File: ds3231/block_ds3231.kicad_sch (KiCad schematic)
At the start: 6 parts, among them U1 DS3231M

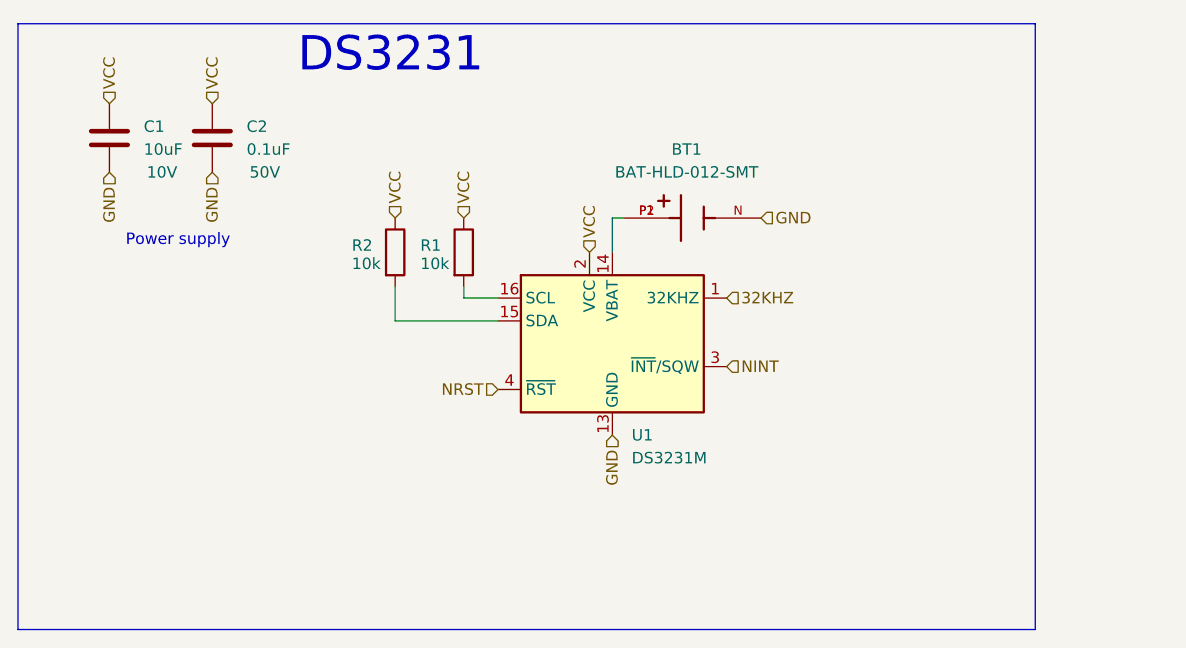
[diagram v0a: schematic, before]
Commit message: [Rushil] corrected pcb added information on both schematic and pcb user drawing correct circuit of bno055
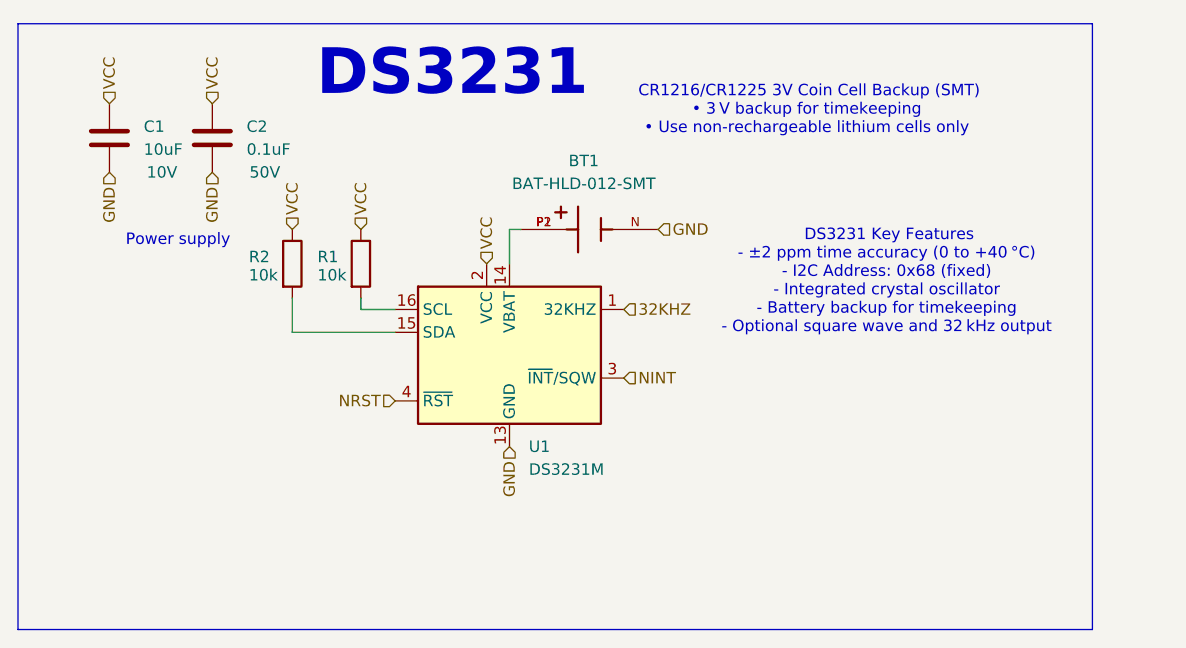
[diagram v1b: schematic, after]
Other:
- note added: "CR1216/CR1225 3V Coin Cell Backup (SMT) • 3 V backup for timekeeping • Use non-rechargeable lithium cells only"
- note added: "DS3231 Key Features - ±2 ppm time accuracy (0 to +40 °C) - I2C Address: 0x68 (fixed) - Integrated crystal oscillator - Battery backup for timekeeping - Optional square wave and 32 kHz output"
- moved on the sheet: BT1, R1, R2, U1
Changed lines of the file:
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@@
 	(rectangle
 		(start 81.28 57.15)
-		(end 194.31 124.46)
+		(end 200.66 124.46)
 		(stroke
 			(width 0)
@@
 		)
 	)
+	(text " DS3231 Key Features  \n- ±2 ppm time accuracy (0 to +40 °C)  \n- I2C Address: 0x68 (fixed)  \n- Integrated crystal oscillator  \n- Battery backup for timekeeping  \n- Optional square wave and 32 kHz output"
+		(exclude_from_sim no)
+		(at 177.8 85.852 0)
+		(effects
+			(font
+				(size 1.27 1.27)
+			)
+		)
+	)
 	(text "Power supply\n"
 		(exclude_from_sim no)
@@
 		)
 	)
-	(text "DS3231\n"
-		(exclude_from_sim no)
-		(at 122.682 60.706 0)
-		(effects
-			(font
-				(size 3.81 3.81)
+	(text " CR1216/CR1225 3V Coin Cell Backup (SMT)\n• 3 V backup for timekeeping  \n• Use non-rechargeable lithium cells only\n"
+		(exclude_from_sim no)
+		(at 168.91 66.802 0)
+		(effects
+			(font
+				(size 1.27 1.27)
+			)
+		)
+	)
+	(text "DS3231"
+		(exclude_from_sim no)
+		(at 129.54 62.738 0)
+		(effects
+			(font
+				(size 5.08 5.08)
+				(thickness 1.016)
+				(bold yes)
 			)
 		)
@@
 	(wire
 		(pts
-			(xy 123.19 90.17) (xy 134.62 90.17)
+			(xy 111.76 91.44) (xy 123.19 91.44)
 		)
 		(stroke
@@
 	(wire
 		(pts
-			(xy 147.32 78.74) (xy 147.32 82.55)
+			(xy 135.89 80.01) (xy 135.89 83.82)
 		)
 		(stroke
@@
 	(wire
 		(pts
-			(xy 148.59 78.74) (xy 147.32 78.74)
+			(xy 137.16 80.01) (xy 135.89 80.01)
 		)
 		(stroke
@@
 	(wire
 		(pts
-			(xy 130.81 87.63) (xy 130.81 86.36)
+			(xy 119.38 88.9) (xy 119.38 87.63)
 		)
 		(stroke
@@
 	(wire
 		(pts
-			(xy 123.19 86.36) (xy 123.19 90.17)
+			(xy 111.76 87.63) (xy 111.76 91.44)
 		)
 		(stroke
@@
 	(wire
 		(pts
-			(xy 130.81 87.63) (xy 134.62 87.63)
+			(xy 119.38 88.9) (xy 123.19 88.9)
 		)
 		(stroke
@@
 	(hierarchical_label "GND"
 		(shape input)
-		(at 147.32 102.87 270)
+		(at 135.89 104.14 270)
 		(effects
 			(font
@@
 	(hierarchical_label "NINT"
 		(shape input)
-		(at 160.02 95.25 0)
+		(at 148.59 96.52 0)
 		(effects
 			(font
@@
 	(hierarchical_label "GND"
 		(shape input)
-		(at 163.83 78.74 0)
+		(at 152.4 80.01 0)
 		(effects
 			(font
@@
 	(hierarchical_label "NRST"
 		(shape input)
-		(at 134.62 97.79 180)
+		(at 123.19 99.06 180)
 		(effects
 			(font
@@
 	(hierarchical_label "VCC"
 		(shape input)
-		(at 144.78 82.55 90)
+		(at 133.35 83.82 90)
 		(effects
 			(font
@@
 	(hierarchical_label "32KHZ"
 		(shape input)
-		(at 160.02 87.63 0)
+		(at 148.59 88.9 0)
 		(effects
 			(font
@@
 	(hierarchical_label "VCC"
 		(shape input)
-		(at 130.81 78.74 90)
+		(at 119.38 80.01 90)
 		(effects
 			(font
@@
 	(hierarchical_label "VCC"
 		(shape input)
-		(at 123.19 78.74 90)
+		(at 111.76 80.01 90)
 		(effects
 			(font
@@
 	(symbol
 		(lib_id "Library:R")
-		(at 123.19 82.55 0)
+		(at 111.76 83.82 0)
 		(unit 1)
 		(exclude_from_sim no)
@@
 		(dnp no)
 		(property "Reference" "R2"
-			(at 118.364 81.788 0)
+			(at 106.934 83.058 0)
 			(effects
 				(font
@@
 		)
 		(property "Value" "10k"
-			(at 118.364 83.82 0)
+			(at 106.934 85.09 0)
 			(effects
 				(font
@@
 		)
 		(property "Footprint" "Resistor_SMD:R_0603_1608Metric"
-			(at 121.412 82.55 90)
+			(at 109.982 83.82 90)
 			(effects
 				(font
@@
 		)
 		(property "Datasheet" "~"
-			(at 123.19 82.55 0)
+			(at 111.76 83.82 0)
 			(effects
 				(font
@@
 		)
 		(property "Description" "Resistor"
-			(at 123.19 82.55 0)
+			(at 111.76 83.82 0)
 			(effects
 				(font
@@
 		)
 		(property "package" "0603"
-			(at 123.19 82.55 0)
+			(at 111.76 83.82 0)
 			(effects
 				(font
@@
 		)
 		(property "LCSC_part#" "C25804"
-			(at 123.19 82.55 0)
+			(at 111.76 83.82 0)
 			(effects
 				(font
@@
 		)
 		(property "MPN" "0603WAF1002T5E"
-			(at 123.19 82.55 0)
+			(at 111.76 83.82 0)
 			(effects
 				(font
@@
 		)
 		(instances
-			(project "ds3231_rtc"
+			(project "ds3231"
 				(path "/2bca7139-9750-4f0a-8cae-c77d5e9ee787/2158ea61-c96a-4c98-b294-c4fdff84ada6"
 					(reference "R2")
@@
 		)
 		(instances
-			(project "ds3231_rtc"
+			(project "ds3231"
 				(path "/2bca7139-9750-4f0a-8cae-c77d5e9ee787/2158ea61-c96a-4c98-b294-c4fdff84ada6"
 					(reference "C1")
@@
 	(symbol
 		(lib_id "Library:R")
-		(at 130.81 82.55 0)
+		(at 119.38 83.82 0)
 		(unit 1)
 		(exclude_from_sim no)
@@
 		(dnp no)
 		(property "Reference" "R1"
-			(at 125.984 81.788 0)
+			(at 114.554 83.058 0)
 			(effects
 				(font
@@
 		)
 		(property "Value" "10k"
-			(at 125.984 83.82 0)
+			(at 114.554 85.09 0)
 			(effects
 				(font
@@
 		)
 		(property "Footprint" "Resistor_SMD:R_0603_1608Metric"
-			(at 129.032 82.55 90)
+			(at 117.602 83.82 90)
 			(effects
 				(font
@@
 		)
 		(property "Datasheet" "~"
-			(at 130.81 82.55 0)
+			(at 119.38 83.82 0)
 			(effects
 				(font
@@
 		)
 		(property "Description" "Resistor"
-			(at 130.81 82.55 0)
+			(at 119.38 83.82 0)
 			(effects
 				(font
@@
 		)
 		(property "package" "0603"
-			(at 130.81 82.55 0)
+			(at 119.38 83.82 0)
 			(effects
 				(font
@@
 		)
 		(property "LCSC_part#" "C25804"
-			(at 130.81 82.55 0)
+			(at 119.38 83.82 0)
 			(effects
 				(font
@@
 		)
 		(property "MPN" "0603WAF1002T5E"
-			(at 130.81 82.55 0)
+			(at 119.38 83.82 0)
 			(effects
 				(font
@@
 		)
 		(instances
-			(project "ds3231_rtc"
+			(project "ds3231"
 				(path "/2bca7139-9750-4f0a-8cae-c77d5e9ee787/2158ea61-c96a-4c98-b294-c4fdff84ada6"
 					(reference "R1")
@@
 		)
 		(instances
-			(project "ds3231_rtc"
+			(project "ds3231"
 				(path "/2bca7139-9750-4f0a-8cae-c77d5e9ee787/2158ea61-c96a-4c98-b294-c4fdff84ada6"
 					(reference "C2")
@@
 	(symbol
 		(lib_id "Library:DS3231M")
-		(at 147.32 92.71 0)
+		(at 135.89 93.98 0)
 		(unit 1)
 		(exclude_from_sim no)
@@
 		(fields_autoplaced yes)
 		(property "Reference" "U1"
-			(at 149.4633 102.87 0)
+			(at 138.0333 104.14 0)
 			(effects
 				(font
@@
 		)
 		(property "Value" "DS3231M"
-			(at 149.4633 105.41 0)
+			(at 138.0333 106.68 0)
 			(effects
 				(font
@@
 		)
 		(property "Footprint" "Package_SO:SOIC-16W_7.5x10.3mm_P1.27mm"
-			(at 147.32 107.95 0)
+			(at 135.89 109.22 0)
 			(effects
 				(font
@@
 		)
 		(property "Datasheet" "http://datasheets.maximintegrated.com/en/ds/DS3231.pdf"
-			(at 154.178 91.44 0)
+			(at 142.748 92.71 0)
 			(effects
 				(font
@@
 		)
 		(property "Description" "Extremely Accurate I2C-Integrated RTC/TCXO/Crystal SOIC-16"
-			(at 147.32 92.71 0)
+			(at 135.89 93.98 0)
 			(effects
 				(font
@@
 		)
 		(property "LCSC_part#" "C37663"
-			(at 147.32 92.71 0)
+			(at 135.89 93.98 0)
 			(effects
 				(font
@@
 		)
 		(property "MPN" "DS3231M+TRL"
-			(at 147.32 92.71 0)
+			(at 135.89 93.98 0)
 			(effects
 				(font
@@
 		)
 		(instances
-			(project ""
+			(project "ds3231"
 				(path "/2bca7139-9750-4f0a-8cae-c77d5e9ee787/2158ea61-c96a-4c98-b294-c4fdff84ada6"
 					(reference "U1")
@@
 	(symbol
 		(lib_id "Library:BAT-HLD-012-SMT")
-		(at 156.21 78.74 0)
+		(at 144.78 80.01 0)
 		(unit 1)
 		(exclude_from_sim no)
@@
 		(fields_autoplaced yes)
 		(property "Reference" "BT1"
-			(at 155.575 71.12 0)
+			(at 144.145 72.39 0)
 			(effects
 				(font
@@
 		)
 		(property "Value" "BAT-HLD-012-SMT"
-			(at 155.575 73.66 0)
+			(at 144.145 74.93 0)
 			(effects
 				(font
@@
 		)
 		(property "Footprint" "BAT-HLD-012-SMT:BAT_BAT-HLD-012-SMT"
-			(at 156.21 78.74 0)
+			(at 144.78 80.01 0)
 			(effects
 				(font
@@
 		)
 		(property "Datasheet" ""
-			(at 156.21 78.74 0)
+			(at 144.78 80.01 0)
 			(effects
 				(font
@@
 		)
 		(property "Description" ""
-			(at 156.21 78.74 0)
+			(at 144.78 80.01 0)
 			(effects
 				(font
@@
 		)
 		(property "LCSC_part#" "C5189234"
-			(at 156.21 78.74 0)
+			(at 144.78 80.01 0)
 			(effects
 				(font
@@
 		)
 		(property "MPN" "BAT-HLD-012-SMT"
-			(at 156.21 78.74 0)
+			(at 144.78 80.01 0)
 			(effects
 				(font
@@
 		)
 		(instances
-			(project ""
+			(project "ds3231"
 				(path "/2bca7139-9750-4f0a-8cae-c77d5e9ee787/2158ea61-c96a-4c98-b294-c4fdff84ada6"
 					(reference "BT1")

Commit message: [Rushil] added ams1117-3.3 block and did some clean up in schematic info part
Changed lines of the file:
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@@
 	(text " DS3231 Key Features  \n- ±2 ppm time accuracy (0 to +40 °C)  \n- I2C Address: 0x68 (fixed)  \n- Integrated crystal oscillator  \n- Battery backup for timekeeping  \n- Optional square wave and 32 kHz output"
 		(exclude_from_sim no)
-		(at 177.8 85.852 0)
+		(at 158.242 89.662 0)
 		(effects
 			(font
 				(size 1.27 1.27)
 			)
+			(justify left)
 		)
 	)
@@
 	(text " CR1216/CR1225 3V Coin Cell Backup (SMT)\n• 3 V backup for timekeeping  \n• Use non-rechargeable lithium cells only\n"
 		(exclude_from_sim no)
-		(at 168.91 66.802 0)
+		(at 155.448 102.108 0)
 		(effects
 			(font
 				(size 1.27 1.27)
 			)
+			(justify left)
 		)
 	)

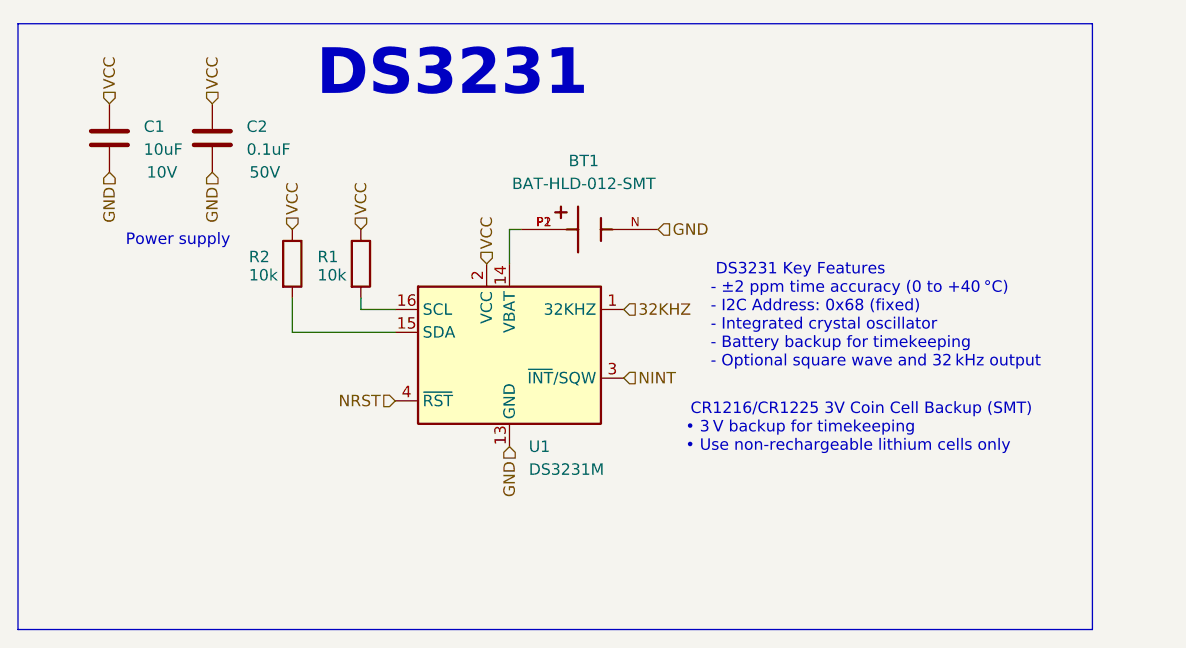
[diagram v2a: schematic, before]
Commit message: Edited and finalized blocks MCP9809 and DS3231
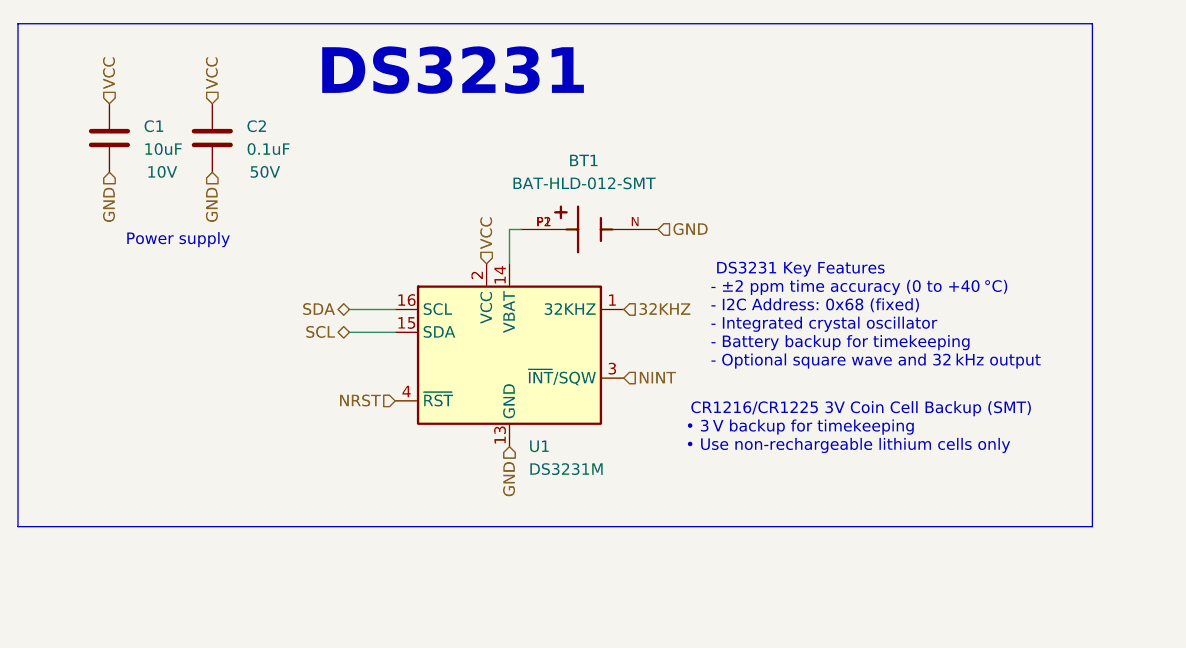
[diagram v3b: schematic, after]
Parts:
- removed R1, R2: 10k, Resistor_SMD:R_0603_1608Metric, symbol Library:R
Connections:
- net SCL: now reaches U1.15 (SDA)
- net SDA: now reaches U1.16 (SCL)
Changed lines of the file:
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@@
 	(rectangle
 		(start 81.28 57.15)
-		(end 200.66 124.46)
+		(end 200.66 113.03)
 		(stroke
 			(width 0)
@@
 	(wire
 		(pts
-			(xy 111.76 91.44) (xy 123.19 91.44)
-		)
-		(stroke
-			(width 0)
-			(type default)
-		)
-	)
-	(wire
-		(pts
 			(xy 135.89 80.01) (xy 135.89 83.82)
 		)
@@
 	(wire
 		(pts
-			(xy 119.38 88.9) (xy 119.38 87.63)
+			(xy 118.11 88.9) (xy 123.19 88.9)
 		)
 		(stroke
@@
 	(wire
 		(pts
-			(xy 111.76 87.63) (xy 111.76 91.44)
-		)
-		(stroke
-			(width 0)
-			(type default)
-		)
-	)
-	(wire
-		(pts
-			(xy 119.38 88.9) (xy 123.19 88.9)
+			(xy 118.11 91.44) (xy 123.19 91.44)
 		)
 		(stroke
@@
 		)
 	)
+	(hierarchical_label "SCL"
+		(shape bidirectional)
+		(at 118.11 91.44 180)
+		(effects
+			(font
+				(size 1.27 1.27)
+			)
+			(justify right)
+		)
+	)
 	(hierarchical_label "GND"
 		(shape input)
@@
 		)
 	)
-	(hierarchical_label "VCC"
-		(shape input)
-		(at 119.38 80.01 90)
-		(effects
-			(font
-				(size 1.27 1.27)
-			)
-			(justify left)
-		)
-	)
-	(hierarchical_label "VCC"
-		(shape input)
-		(at 111.76 80.01 90)
-		(effects
-			(font
-				(size 1.27 1.27)
-			)
-			(justify left)
-		)
-	)
-	(symbol
-		(lib_id "Library:R")
-		(at 111.76 83.82 0)
-		(unit 1)
-		(exclude_from_sim no)
-		(in_bom yes)
-		(on_board yes)
-		(dnp no)
-		(property "Reference" "R2"
-			(at 106.934 83.058 0)
-			(effects
-				(font
-					(size 1.27 1.27)
-				)
-				(justify left)
-			)
-		)
-		(property "Value" "10k"
-			(at 106.934 85.09 0)
-			(effects
-				(font
-					(size 1.27 1.27)
-				)
-				(justify left)
-			)
-		)
-		(property "Footprint" "Resistor_SMD:R_0603_1608Metric"
-			(at 109.982 83.82 90)
-			(effects
-				(font
-					(size 1.27 1.27)
-				)
-				(hide yes)
-			)
-		)
-		(property "Datasheet" "~"
-			(at 111.76 83.82 0)
-			(effects
-				(font
-					(size 1.27 1.27)
-				)
-				(hide yes)
-			)
-		)
-		(property "Description" "Resistor"
-			(at 111.76 83.82 0)
-			(effects
-				(font
-					(size 1.27 1.27)
-				)
-				(hide yes)
-			)
-		)
-		(property "package" "0603"
-			(at 111.76 83.82 0)
-			(effects
-				(font
-					(size 1.27 1.27)
-				)
-				(hide yes)
-			)
-		)
-		(property "LCSC_part#" "C25804"
-			(at 111.76 83.82 0)
-			(effects
-				(font
-					(size 1.27 1.27)
-				)
-				(hide yes)
-			)
-		)
-		(property "MPN" "0603WAF1002T5E"
-			(at 111.76 83.82 0)
-			(effects
-				(font
-					(size 1.27 1.27)
-				)
-				(hide yes)
-			)
-		)
-		(pin "2"
-		)
-		(pin "1"
-		)
-		(instances
-			(project "ds3231"
-				(path "/2bca7139-9750-4f0a-8cae-c77d5e9ee787/2158ea61-c96a-4c98-b294-c4fdff84ada6"
-					(reference "R2")
-					(unit 1)
-				)
-			)
+	(hierarchical_label "SDA"
+		(shape bidirectional)
+		(at 118.11 88.9 180)
+		(effects
+			(font
+				(size 1.27 1.27)
+			)
+			(justify right)
 		)
 	)
@@
 					(unit 1)
 				)
-			)
-		)
-	)
-	(symbol
-		(lib_id "Library:R")
-		(at 119.38 83.82 0)
-		(unit 1)
-		(exclude_from_sim no)
-		(in_bom yes)
-		(on_board yes)
-		(dnp no)
-		(property "Reference" "R1"
-			(at 114.554 83.058 0)
-			(effects
-				(font
-					(size 1.27 1.27)
-				)
-				(justify left)
-			)
-		)
-		(property "Value" "10k"
-			(at 114.554 85.09 0)
-			(effects
-				(font
-					(size 1.27 1.27)
-				)
-				(justify left)
-			)
-		)
-		(property "Footprint" "Resistor_SMD:R_0603_1608Metric"
-			(at 117.602 83.82 90)
-			(effects
-				(font
-					(size 1.27 1.27)
-				)
-				(hide yes)
-			)
-		)
-		(property "Datasheet" "~"
-			(at 119.38 83.82 0)
-			(effects
-				(font
-					(size 1.27 1.27)
-				)
-				(hide yes)
-			)
-		)
-		(property "Description" "Resistor"
-			(at 119.38 83.82 0)
-			(effects
-				(font
-					(size 1.27 1.27)
-				)
-				(hide yes)
-			)
-		)
-		(property "package" "0603"
-			(at 119.38 83.82 0)
-			(effects
-				(font
-					(size 1.27 1.27)
-				)
-				(hide yes)
-			)
-		)
-		(property "LCSC_part#" "C25804"
-			(at 119.38 83.82 0)
-			(effects
-				(font
-					(size 1.27 1.27)
-				)
-				(hide yes)
-			)
-		)
-		(property "MPN" "0603WAF1002T5E"
-			(at 119.38 83.82 0)
-			(effects
-				(font
-					(size 1.27 1.27)
-				)
-				(hide yes)
-			)
-		)
-		(pin "2"
-		)
-		(pin "1"
-		)
-		(instances
-			(project "ds3231"
-				(path "/2bca7139-9750-4f0a-8cae-c77d5e9ee787/2158ea61-c96a-4c98-b294-c4fdff84ada6"
-					(reference "R1")
-					(unit 1)
-				)
